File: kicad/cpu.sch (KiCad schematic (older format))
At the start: 13 parts, among them P2 SWD, U5 LPC1227FBD48/301, Y2 32.768k 12.5p

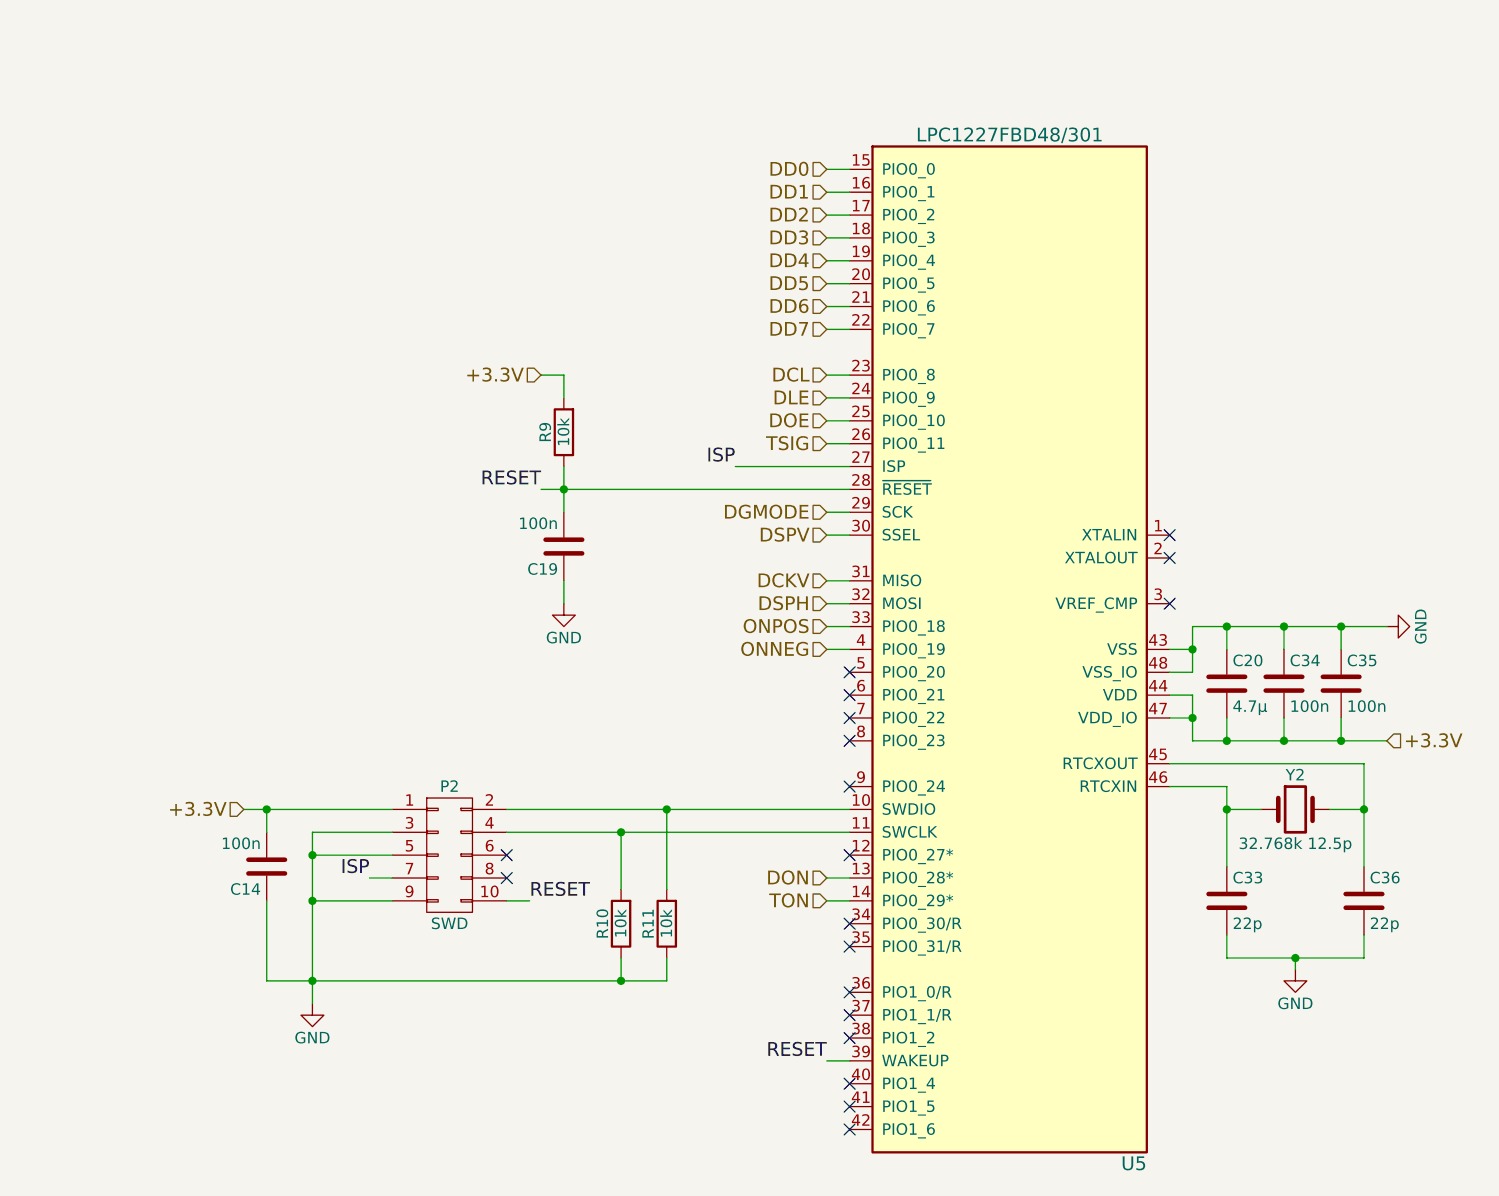
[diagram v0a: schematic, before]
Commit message: Finish schematic
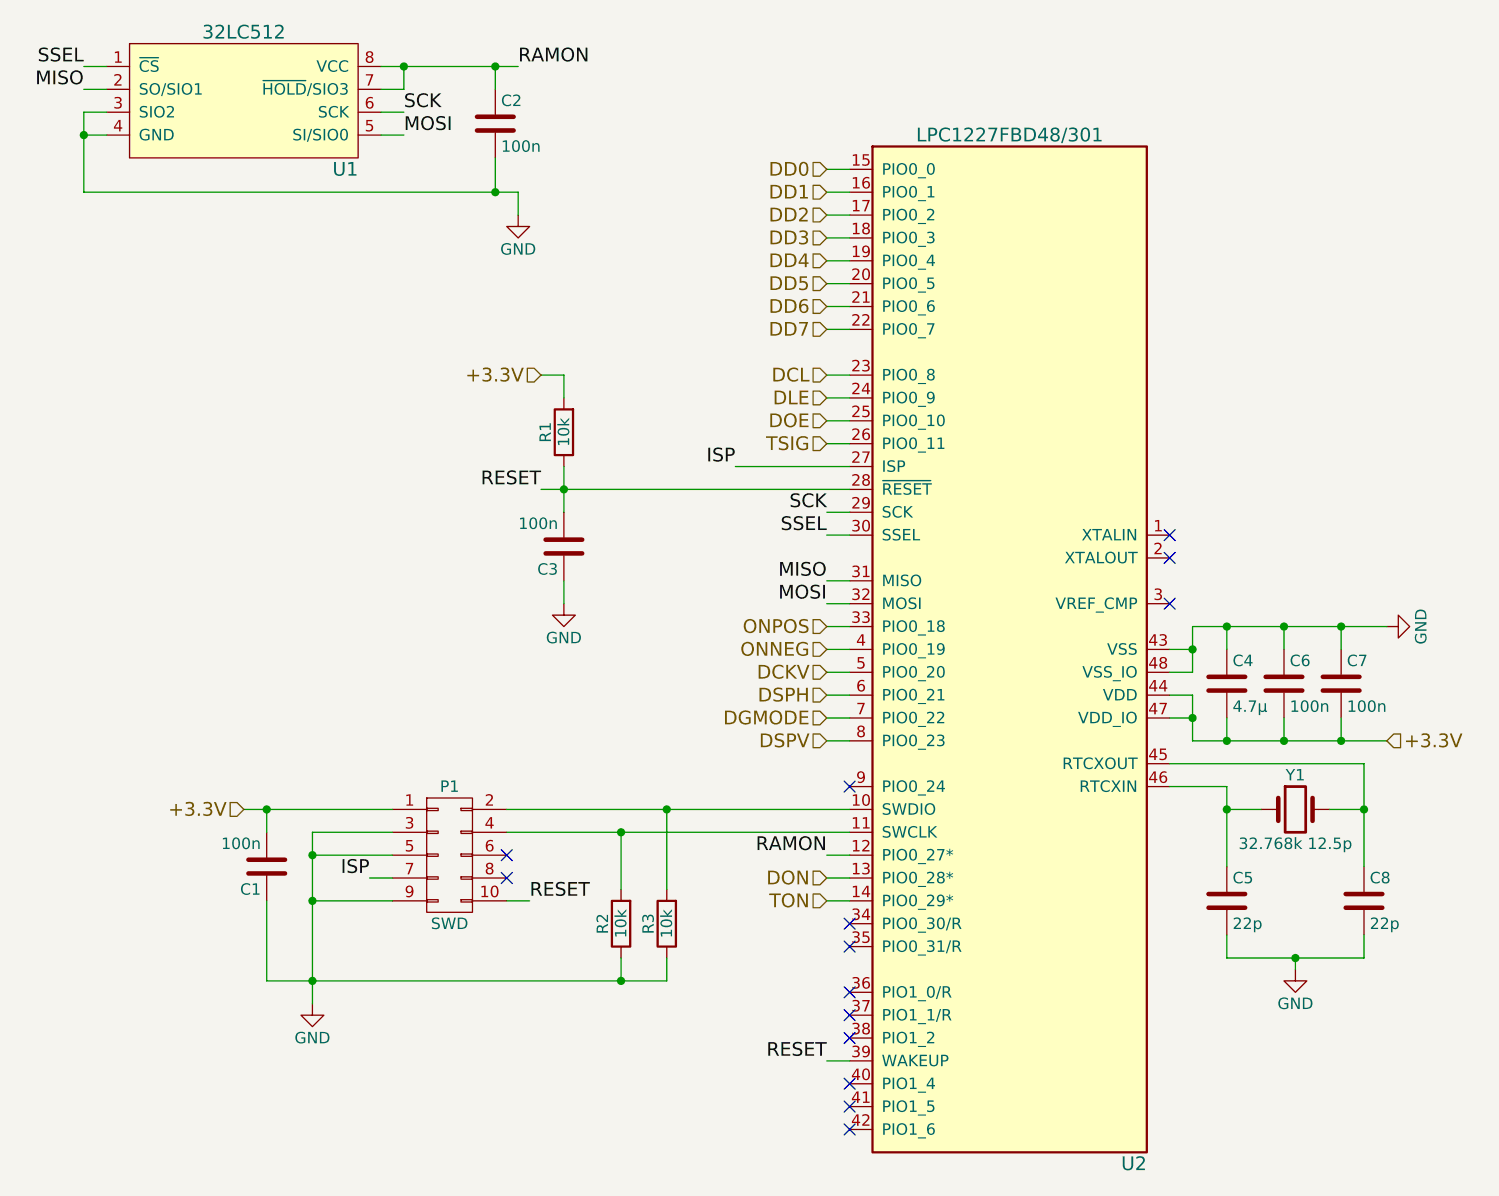
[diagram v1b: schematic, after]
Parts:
- added C2: 100n, symbol C
- added U1: 32LC512, symbol 32LC512
- renumbered C14 to C1, C19 to C3, C20 to C4, C33 to C5, C34 to C6, C35 to C7, C36 to C8, P2 to P1, R9 to R1, R10 to R2, R11 to R3, U5 to U2, Y2 to Y1
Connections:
- net DCKV: now also U2.5 (PIO0_20); no longer U2.31 (MISO)
- net DGMODE: now also U2.7 (PIO0_22); no longer U2.29 (SCK)
- net DSPH: now also U2.6 (PIO0_21); no longer U2.32 (MOSI)
- net DSPV: now also U2.8 (PIO0_23); no longer U2.30 (SSEL)
- net GND: now also C2.2, U1.3 (SIO2), U1.4 (GND)
- net RAMON: now reaches U2.12 (PIO0_27*)
- net RAMON: now also C2.1, U1.7 (~HOLD~/SIO3), U1.8 (VCC)
- new net MISO: U1.2 (SO/SIO1), U2.31 (MISO)
- new net MOSI: U1.5 (SI/SIO0), U2.32 (MOSI)
- new net SCK: U1.6 (SCK), U2.29 (SCK)
- new net SSEL: U1.1 (~CS), U2.30 (SSEL)
- no-connect marks 19 -> 14
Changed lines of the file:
@@
 $Descr A4 11693 8268
 encoding utf-8
-Sheet 4 5
-Title ""
-Date ""
-Rev ""
+Sheet 2 5
+Title "E-Ink Clock"
+Date "2017-03-29"
+Rev "1.0"
 Comp ""
 Comment1 ""
@@
 $EndDescr
 $Comp
-L LPC1227FBD48/301 U5
+L LPC1227FBD48/301 U2
 U 1 1 58DEBAB0
 P 5500 3600
-F 0 "U5" H 6100 1350 60  0000 R CNN
+F 0 "U2" H 6100 1350 60  0000 R CNN
 F 1 "LPC1227FBD48/301" H 5500 5850 60  0000 C CNN
 F 2 "" H 5300 4850 60  0001 C CNN
@@
 NoConn ~ 4800 4900
 NoConn ~ 4800 4800
-NoConn ~ 4800 3800
-$Comp
-L C C34
+$Comp
+L C C6
 U 1 1 58DEBAD4
 P 6700 3750
-F 0 "C34" H 6725 3850 50  0000 L CNN
+F 0 "C6" H 6725 3850 50  0000 L CNN
 F 1 "100n" H 6725 3650 50  0000 L CNN
 F 2 "" H 6738 3600 50  0001 C CNN
@@
 $EndComp
 $Comp
-L C C35
+L C C7
 U 1 1 58DEBADB
 P 6950 3750
-F 0 "C35" H 6975 3850 50  0000 L CNN
+F 0 "C7" H 6975 3850 50  0000 L CNN
 F 1 "100n" H 6975 3650 50  0000 L CNN
 F 2 "" H 6988 3600 50  0001 C CNN
@@
 $EndComp
 $Comp
-L GND #PWR02
+L GND #PWR6
 U 1 1 58DEBAE8
 P 7150 3500
-F 0 "#PWR02" H 7150 3250 50  0001 C CNN
+F 0 "#PWR6" H 7150 3250 50  0001 C CNN
 F 1 "GND" H 7150 3350 50  0000 C CNN
 F 2 "" H 7150 3500 50  0000 C CNN
@@
 $EndComp
 $Comp
-L Crystal Y2
+L Crystal Y1
 U 1 1 58DEBAEE
 P 6750 4300
-F 0 "Y2" H 6750 4450 50  0000 C CNN
+F 0 "Y1" H 6750 4450 50  0000 C CNN
 F 1 "32.768k 12.5p" H 6750 4150 50  0000 C CNN
 F 2 "" H 6750 4300 50  0001 C CNN
@@
 $EndComp
 $Comp
-L C C33
+L C C5
 U 1 1 58DEBAF5
 P 6450 4700
-F 0 "C33" H 6475 4800 50  0000 L CNN
+F 0 "C5" H 6475 4800 50  0000 L CNN
 F 1 "22p" H 6475 4600 50  0000 L CNN
 F 2 "" H 6488 4550 50  0001 C CNN
@@
 $EndComp
 $Comp
-L C C36
+L C C8
 U 1 1 58DEBAFC
 P 7050 4700
-F 0 "C36" H 7075 4800 50  0000 L CNN
+F 0 "C8" H 7075 4800 50  0000 L CNN
 F 1 "22p" H 7075 4600 50  0000 L CNN
 F 2 "" H 7088 4550 50  0001 C CNN
@@
 $EndComp
 $Comp
-L GND #PWR03
+L GND #PWR5
 U 1 1 58DEBB03
 P 6750 5000
-F 0 "#PWR03" H 6750 4750 50  0001 C CNN
+F 0 "#PWR5" H 6750 4750 50  0001 C CNN
 F 1 "GND" H 6750 4850 50  0000 C CNN
 F 2 "" H 6750 5000 50  0000 C CNN
@@
 $EndComp
 $Comp
-L CONN_02X05 P2
+L CONN_02X05 P1
 U 1 1 58DEBB09
 P 3050 4500
-F 0 "P2" H 3050 4800 50  0000 C CNN
+F 0 "P1" H 3050 4800 50  0000 C CNN
 F 1 "SWD" H 3050 4200 50  0000 C CNN
 F 2 "" H 3050 3300 50  0001 C CNN
@@
 $EndComp
 $Comp
-L R R9
+L R R1
 U 1 1 58DEBB16
 P 3550 2650
-F 0 "R9" V 3630 2650 50  0000 C CNN
+F 0 "R1" V 3630 2650 50  0000 C CNN
 F 1 "10k" V 3550 2650 50  0000 C CNN
 F 2 "" V 3480 2650 50  0001 C CNN
@@
 $EndComp
 $Comp
-L GND #PWR04
+L GND #PWR2
 U 1 1 58DEBB1D
 P 2450 5150
-F 0 "#PWR04" H 2450 4900 50  0001 C CNN
+F 0 "#PWR2" H 2450 4900 50  0001 C CNN
 F 1 "GND" H 2450 5000 50  0000 C CNN
 F 2 "" H 2450 5150 50  0000 C CNN
@@
 NoConn ~ 3300 4600
 $Comp
-L C C14
+L C C1
 U 1 1 58DEBB24
 P 2250 4550
-F 0 "C14" H 2275 4650 50  0000 L CNN
+F 0 "C1" H 2275 4650 50  0000 L CNN
 F 1 "100n" H 2275 4450 50  0000 L CNN
 F 2 "" H 2288 4400 50  0001 C CNN
@@
 $EndComp
 $Comp
-L C C19
+L C C3
 U 1 1 58DEBB2B
 P 3550 3150
-F 0 "C19" H 3575 3250 50  0000 L CNN
+F 0 "C3" H 3575 3250 50  0000 L CNN
 F 1 "100n" H 3575 3050 50  0000 L CNN
 F 2 "" H 3588 3000 50  0001 C CNN
@@
 $EndComp
 $Comp
-L GND #PWR05
+L GND #PWR4
 U 1 1 58DEBB38
 P 3550 3400
-F 0 "#PWR05" H 3550 3150 50  0001 C CNN
+F 0 "#PWR4" H 3550 3150 50  0001 C CNN
 F 1 "GND" H 3550 3250 50  0000 C CNN
 F 2 "" H 3550 3400 50  0000 C CNN
@@
 NoConn ~ 6200 3200
 NoConn ~ 6200 3400
-NoConn ~ 4800 3700
 NoConn ~ 3300 4500
 Wire Wire Line
@@
 	4700 4600 4800 4600
 $Comp
-L R R10
+L R R2
 U 1 1 58DEBBA3
 P 3800 4800
-F 0 "R10" V 3880 4800 50  0000 C CNN
+F 0 "R2" V 3880 4800 50  0000 C CNN
 F 1 "10k" V 3800 4800 50  0000 C CNN
 F 2 "" V 3730 4800 50  0001 C CNN
@@
 $EndComp
 $Comp
-L R R11
+L R R3
 U 1 1 58DEBBAA
 P 4000 4800
-F 0 "R11" V 4080 4800 50  0000 C CNN
+F 0 "R3" V 4080 4800 50  0000 C CNN
 F 1 "10k" V 4000 4800 50  0000 C CNN
 F 2 "" V 3930 4800 50  0001 C CNN
@@
 Wire Wire Line
 	4700 3400 4800 3400
-NoConn ~ 4800 3900
-NoConn ~ 4800 4000
 NoConn ~ 4800 4200
-NoConn ~ 4800 4500
-$Comp
-L C C20
+$Comp
+L C C4
 U 1 1 58DEBBC8
 P 6450 3750
-F 0 "C20" H 6475 3850 50  0000 L CNN
+F 0 "C4" H 6475 3850 50  0000 L CNN
 F 1 "4.7µ" H 6475 3650 50  0000 L CNN
 F 2 "" H 6488 3600 50  0001 C CNN
@@
 Text HLabel 7150 4000 2    60   Input ~ 0
 +3.3V
-Text HLabel 4700 3000 0    60   Input ~ 0
+Text HLabel 4700 3900 0    60   Input ~ 0
 DGMODE
-Text HLabel 4700 3100 0    60   Input ~ 0
+Text HLabel 4700 4000 0    60   Input ~ 0
 DSPV
-Text HLabel 4700 3300 0    60   Input ~ 0
+Text HLabel 4700 3700 0    60   Input ~ 0
 DCKV
-Text HLabel 4700 3400 0    60   Input ~ 0
+Text HLabel 4700 3800 0    60   Input ~ 0
 DSPH
 Text HLabel 4700 3500 0    60   Input ~ 0
@@
 Connection ~ 3800 5050
 Connection ~ 2450 5050
+Wire Wire Line
+	4800 4000 4700 4000
+Wire Wire Line
+	4800 3900 4700 3900
+Wire Wire Line
+	4800 3800 4700 3800
+Wire Wire Line
+	4800 3700 4700 3700
+Text Label 4700 3000 2    60   ~ 0
+SCK
+Text Label 4700 3100 2    60   ~ 0
+SSEL
+Text Label 4700 3400 2    60   ~ 0
+MOSI
+Text Label 4700 3300 2    60   ~ 0
+MISO
+$Comp
+L 32LC512 U1
+U 1 1 58DE0750
+P 2150 1200
+F 0 "U1" H 2650 900 60  0000 R CNN
+F 1 "32LC512" H 2150 1500 60  0000 C CNN
+F 2 "" H 2150 1200 60  0001 C CNN
+F 3 "" H 2150 1200 60  0001 C CNN
+	1    2150 1200
+	1    0    0    -1
+$EndComp
+Text Label 4700 4500 2    60   ~ 0
+RAMON
+Wire Wire Line
+	4700 4500 4800 4500
+Text Label 3350 1050 0    60   ~ 0
+RAMON
+Text Label 2850 1350 0    60   ~ 0
+MOSI
+Text Label 1450 1150 2    60   ~ 0
+MISO
+Text Label 1450 1050 2    60   ~ 0
+SSEL
+Text Label 2850 1250 0    60   ~ 0
+SCK
+$Comp
+L GND #PWR3
+U 1 1 58DE0BD2
+P 3350 1700
+F 0 "#PWR3" H 3350 1450 50  0001 C CNN
+F 1 "GND" H 3350 1550 50  0000 C CNN
+F 2 "" H 3350 1700 50  0000 C CNN
+F 3 "" H 3350 1700 50  0000 C CNN
+	1    3350 1700
+	1    0    0    -1
+$EndComp
+Wire Wire Line
+	1550 1350 1450 1350
+Wire Wire Line
+	1450 1250 1450 1600
+Wire Wire Line
+	1450 1600 3350 1600
+Wire Wire Line
+	1550 1250 1450 1250
+Connection ~ 1450 1350
+Wire Wire Line
+	2750 1050 3350 1050
+Wire Wire Line
+	2850 1050 2850 1150
+Wire Wire Line
+	2850 1150 2750 1150
+Connection ~ 2850 1050
+$Comp
+L C C2
+U 1 1 58DE1215
+P 3250 1300
+F 0 "C2" H 3275 1400 50  0000 L CNN
+F 1 "100n" H 3275 1200 50  0000 L CNN
+F 2 "" H 3288 1150 50  0001 C CNN
+F 3 "" H 3250 1300 50  0001 C CNN
+	1    3250 1300
+	1    0    0    -1
+$EndComp
+Wire Wire Line
+	3350 1600 3350 1700
+Wire Wire Line
+	3250 1600 3250 1450
+Connection ~ 3250 1600
+Wire Wire Line
+	3250 1150 3250 1050
+Connection ~ 3250 1050
+Wire Wire Line
+	1450 1050 1550 1050
+Wire Wire Line
+	2850 1250 2750 1250
+Wire Wire Line
+	2850 1350 2750 1350
+Wire Wire Line
+	1450 1150 1550 1150
 $EndSCHEMATC

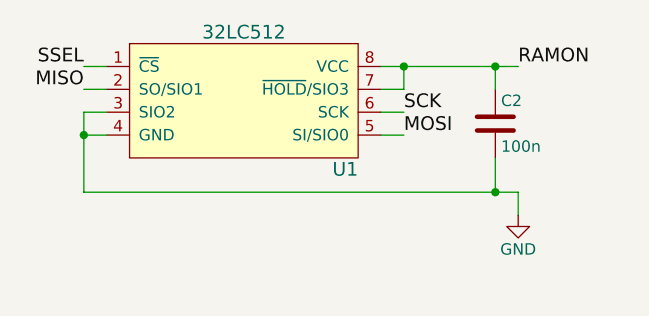
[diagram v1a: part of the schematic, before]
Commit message: Set most footprints
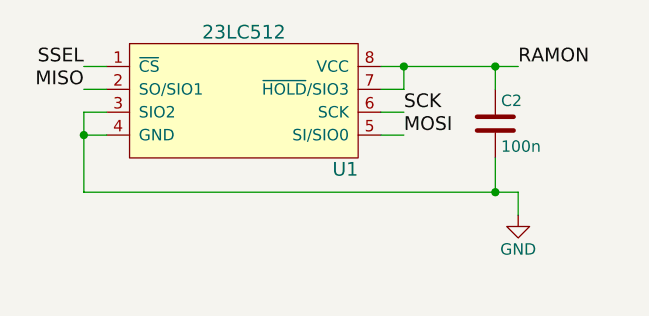
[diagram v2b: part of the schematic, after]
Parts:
- removed U1: 32LC512, symbol 32LC512
- added U1: 23LC512, Housings_SOIC:SOIC-8_3.9x4.9mm_Pitch1.27mm, symbol 23LC512
- C1, C2, C3, C4, C5, C6, C7, C8: footprint (none) -> Capacitors_SMD:C_0805_HandSoldering
- R1, R2, R3: footprint (none) -> Resistors_SMD:R_0805_HandSoldering
- U2: footprint (none) -> Housings_QFP:LQFP-48_7x7mm_Pitch0.5mm
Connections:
- net GND: now also U1.3 (SIO2), U1.4 (GND)
- net MISO: now also U1.2 (SO/SIO1)
- net MOSI: now also U1.5 (SI/SIO0)
- net RAMON: now also U1.7 (~HOLD~/SIO3), U1.8 (VCC)
- net SCK: now also U1.6 (SCK)
- net SSEL: now also U1.1 (~CS)
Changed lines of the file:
@@
 F 0 "U2" H 6100 1350 60  0000 R CNN
 F 1 "LPC1227FBD48/301" H 5500 5850 60  0000 C CNN
-F 2 "" H 5300 4850 60  0001 C CNN
+F 2 "Housings_QFP:LQFP-48_7x7mm_Pitch0.5mm" H 5300 4850 60  0001 C CNN
 F 3 "" H 5300 4850 60  0001 C CNN
 	1    5500 3600
@@
 F 0 "C6" H 6725 3850 50  0000 L CNN
 F 1 "100n" H 6725 3650 50  0000 L CNN
-F 2 "" H 6738 3600 50  0001 C CNN
+F 2 "Capacitors_SMD:C_0805_HandSoldering" H 6738 3600 50  0001 C CNN
 F 3 "" H 6700 3750 50  0000 C CNN
 	1    6700 3750
@@
 F 0 "C7" H 6975 3850 50  0000 L CNN
 F 1 "100n" H 6975 3650 50  0000 L CNN
-F 2 "" H 6988 3600 50  0001 C CNN
+F 2 "Capacitors_SMD:C_0805_HandSoldering" H 6988 3600 50  0001 C CNN
 F 3 "" H 6950 3750 50  0000 C CNN
 	1    6950 3750
@@
 $EndComp
 $Comp
-L GND #PWR6
+L GND #PWR02
 U 1 1 58DEBAE8
 P 7150 3500
-F 0 "#PWR6" H 7150 3250 50  0001 C CNN
+F 0 "#PWR02" H 7150 3250 50  0001 C CNN
 F 1 "GND" H 7150 3350 50  0000 C CNN
 F 2 "" H 7150 3500 50  0000 C CNN
@@
 F 0 "C5" H 6475 4800 50  0000 L CNN
 F 1 "22p" H 6475 4600 50  0000 L CNN
-F 2 "" H 6488 4550 50  0001 C CNN
+F 2 "Capacitors_SMD:C_0805_HandSoldering" H 6488 4550 50  0001 C CNN
 F 3 "" H 6450 4700 50  0000 C CNN
 	1    6450 4700
@@
 F 0 "C8" H 7075 4800 50  0000 L CNN
 F 1 "22p" H 7075 4600 50  0000 L CNN
-F 2 "" H 7088 4550 50  0001 C CNN
+F 2 "Capacitors_SMD:C_0805_HandSoldering" H 7088 4550 50  0001 C CNN
 F 3 "" H 7050 4700 50  0000 C CNN
 	1    7050 4700
@@
 $EndComp
 $Comp
-L GND #PWR5
+L GND #PWR03
 U 1 1 58DEBB03
 P 6750 5000
-F 0 "#PWR5" H 6750 4750 50  0001 C CNN
+F 0 "#PWR03" H 6750 4750 50  0001 C CNN
 F 1 "GND" H 6750 4850 50  0000 C CNN
 F 2 "" H 6750 5000 50  0000 C CNN
@@
 F 0 "R1" V 3630 2650 50  0000 C CNN
 F 1 "10k" V 3550 2650 50  0000 C CNN
-F 2 "" V 3480 2650 50  0001 C CNN
+F 2 "Resistors_SMD:R_0805_HandSoldering" V 3480 2650 50  0001 C CNN
 F 3 "" H 3550 2650 50  0000 C CNN
 	1    3550 2650
@@
 $EndComp
 $Comp
-L GND #PWR2
+L GND #PWR04
 U 1 1 58DEBB1D
 P 2450 5150
-F 0 "#PWR2" H 2450 4900 50  0001 C CNN
+F 0 "#PWR04" H 2450 4900 50  0001 C CNN
 F 1 "GND" H 2450 5000 50  0000 C CNN
 F 2 "" H 2450 5150 50  0000 C CNN
@@
 F 0 "C1" H 2275 4650 50  0000 L CNN
 F 1 "100n" H 2275 4450 50  0000 L CNN
-F 2 "" H 2288 4400 50  0001 C CNN
+F 2 "Capacitors_SMD:C_0805_HandSoldering" H 2288 4400 50  0001 C CNN
 F 3 "" H 2250 4550 50  0000 C CNN
 	1    2250 4550
@@
 F 0 "C3" H 3575 3250 50  0000 L CNN
 F 1 "100n" H 3575 3050 50  0000 L CNN
-F 2 "" H 3588 3000 50  0001 C CNN
+F 2 "Capacitors_SMD:C_0805_HandSoldering" H 3588 3000 50  0001 C CNN
 F 3 "" H 3550 3150 50  0000 C CNN
 	1    3550 3150
@@
 $EndComp
 $Comp
-L GND #PWR4
+L GND #PWR05
 U 1 1 58DEBB38
 P 3550 3400
-F 0 "#PWR4" H 3550 3150 50  0001 C CNN
+F 0 "#PWR05" H 3550 3150 50  0001 C CNN
 F 1 "GND" H 3550 3250 50  0000 C CNN
 F 2 "" H 3550 3400 50  0000 C CNN
@@
 F 0 "R2" V 3880 4800 50  0000 C CNN
 F 1 "10k" V 3800 4800 50  0000 C CNN
-F 2 "" V 3730 4800 50  0001 C CNN
+F 2 "Resistors_SMD:R_0805_HandSoldering" V 3730 4800 50  0001 C CNN
 F 3 "" H 3800 4800 50  0000 C CNN
 	1    3800 4800
@@
 F 0 "R3" V 4080 4800 50  0000 C CNN
 F 1 "10k" V 4000 4800 50  0000 C CNN
-F 2 "" V 3930 4800 50  0001 C CNN
+F 2 "Resistors_SMD:R_0805_HandSoldering" V 3930 4800 50  0001 C CNN
 F 3 "" H 4000 4800 50  0000 C CNN
 	1    4000 4800
@@
 F 0 "C4" H 6475 3850 50  0000 L CNN
 F 1 "4.7µ" H 6475 3650 50  0000 L CNN
-F 2 "" H 6488 3600 50  0001 C CNN
+F 2 "Capacitors_SMD:C_0805_HandSoldering" H 6488 3600 50  0001 C CNN
 F 3 "" H 6450 3750 50  0000 C CNN
 	1    6450 3750
@@
 Text Label 4700 3300 2    60   ~ 0
 MISO
-$Comp
-L 32LC512 U1
-U 1 1 58DE0750
-P 2150 1200
-F 0 "U1" H 2650 900 60  0000 R CNN
-F 1 "32LC512" H 2150 1500 60  0000 C CNN
-F 2 "" H 2150 1200 60  0001 C CNN
-F 3 "" H 2150 1200 60  0001 C CNN
-	1    2150 1200
-	1    0    0    -1
-$EndComp
 Text Label 4700 4500 2    60   ~ 0
 RAMON
@@
 SCK
 $Comp
-L GND #PWR3
+L GND #PWR06
 U 1 1 58DE0BD2
 P 3350 1700
-F 0 "#PWR3" H 3350 1450 50  0001 C CNN
+F 0 "#PWR06" H 3350 1450 50  0001 C CNN
 F 1 "GND" H 3350 1550 50  0000 C CNN
 F 2 "" H 3350 1700 50  0000 C CNN
@@
 F 0 "C2" H 3275 1400 50  0000 L CNN
 F 1 "100n" H 3275 1200 50  0000 L CNN
-F 2 "" H 3288 1150 50  0001 C CNN
+F 2 "Capacitors_SMD:C_0805_HandSoldering" H 3288 1150 50  0001 C CNN
 F 3 "" H 3250 1300 50  0001 C CNN
 	1    3250 1300
@@
 Wire Wire Line
 	1450 1150 1550 1150
+$Comp
+L 23LC512 U1
+U 1 1 58DE78DA
+P 2150 1200
+F 0 "U1" H 2650 900 60  0000 R CNN
+F 1 "23LC512" H 2150 1500 60  0000 C CNN
+F 2 "Housings_SOIC:SOIC-8_3.9x4.9mm_Pitch1.27mm" H 2150 1200 60  0001 C CNN
+F 3 "" H 2150 1200 60  0001 C CNN
+	1    2150 1200
+	1    0    0    -1
+$EndComp
 $EndSCHEMATC

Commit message: Finish footprints
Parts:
- P1: footprint (none) -> Connectors:IDC_Header_Straight_10pins
- Y1: footprint (none) -> einkclock:Crystal_Lying_1
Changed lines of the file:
@@
 F 0 "Y1" H 6750 4450 50  0000 C CNN
 F 1 "32.768k 12.5p" H 6750 4150 50  0000 C CNN
-F 2 "" H 6750 4300 50  0001 C CNN
+F 2 "einkclock:Crystal_Lying_1" H 6750 4300 50  0001 C CNN
 F 3 "" H 6750 4300 50  0000 C CNN
 	1    6750 4300
@@
 F 0 "P1" H 3050 4800 50  0000 C CNN
 F 1 "SWD" H 3050 4200 50  0000 C CNN
-F 2 "" H 3050 3300 50  0001 C CNN
+F 2 "Connectors:IDC_Header_Straight_10pins" H 3050 3300 50  0001 C CNN
 F 3 "" H 3050 3300 50  0000 C CNN
 	1    3050 4500
